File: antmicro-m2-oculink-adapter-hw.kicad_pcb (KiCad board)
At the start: 4 copper layers, 22 x 80 mm, 24 parts, among them J1 PCB-Edge_M.2_Key-M, J2 OCuLink_x4_Amphenol_G14A42121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

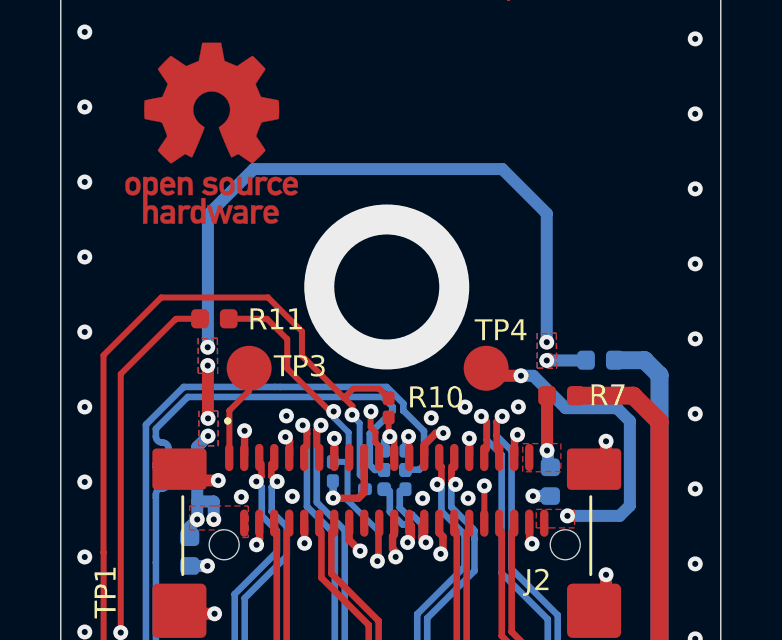
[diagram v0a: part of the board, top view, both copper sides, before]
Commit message: [#81131] Add 0R on 5V, Clean drc
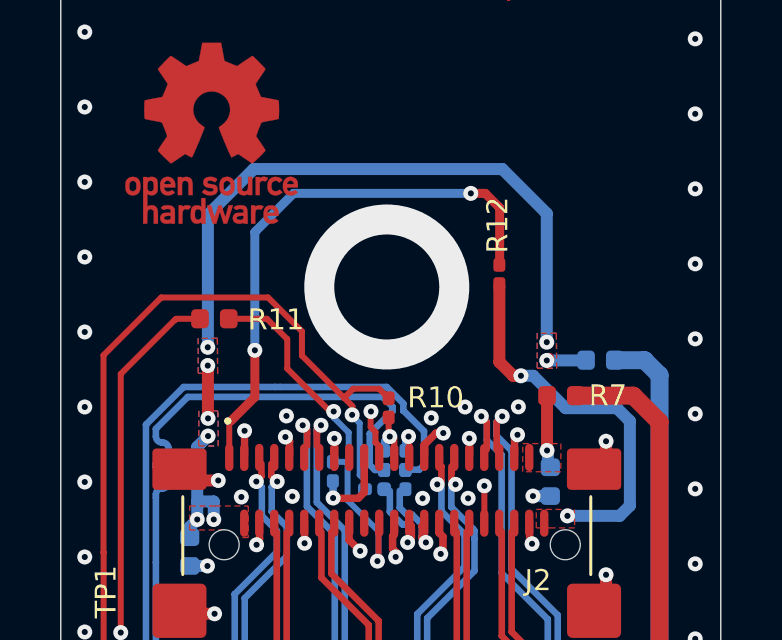
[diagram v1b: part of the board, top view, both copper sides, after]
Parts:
- removed TP3, TP4: TP_1.5mm_SMD, antmicro-footprints:TP_SMD_1.5mm
- added R12: R_0R_0201, antmicro-footprints:R_0201, F.Cu at (149.8, 88.2)
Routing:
- net Net-(J2-5V-PadA21): track 13.8 -> 31.4 mm, vias 2 -> 4

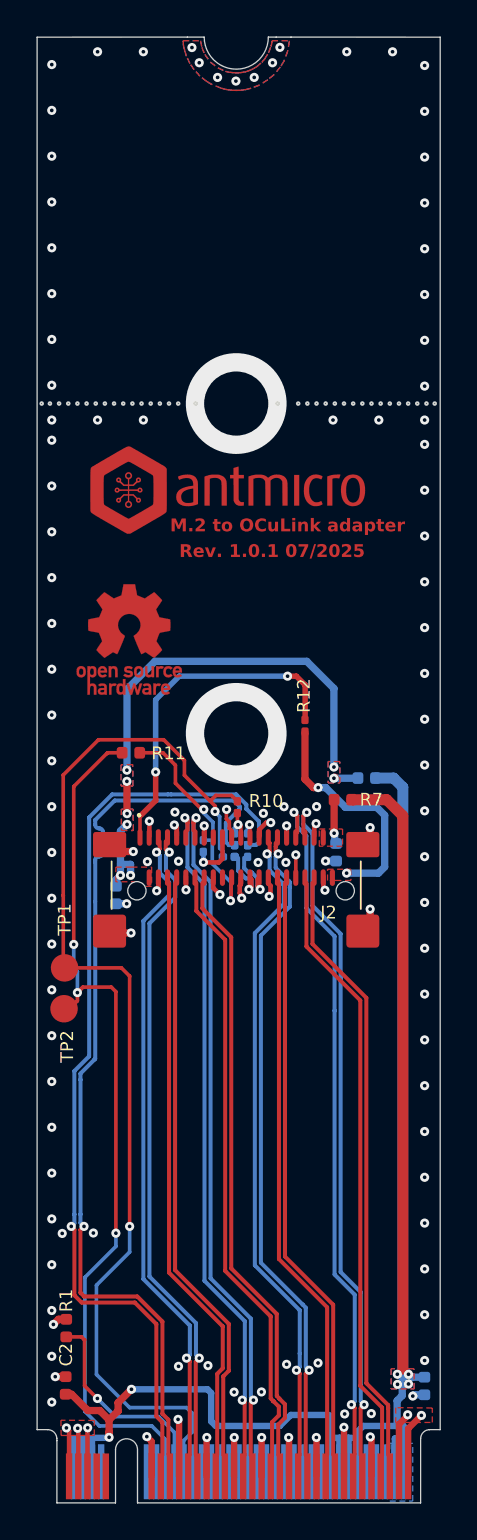
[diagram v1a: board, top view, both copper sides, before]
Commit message: [#81131] Increase silkscreen spacing, add gnd cutouts to vias, increase distance drill to traces, remove solder mask from m.2 connector
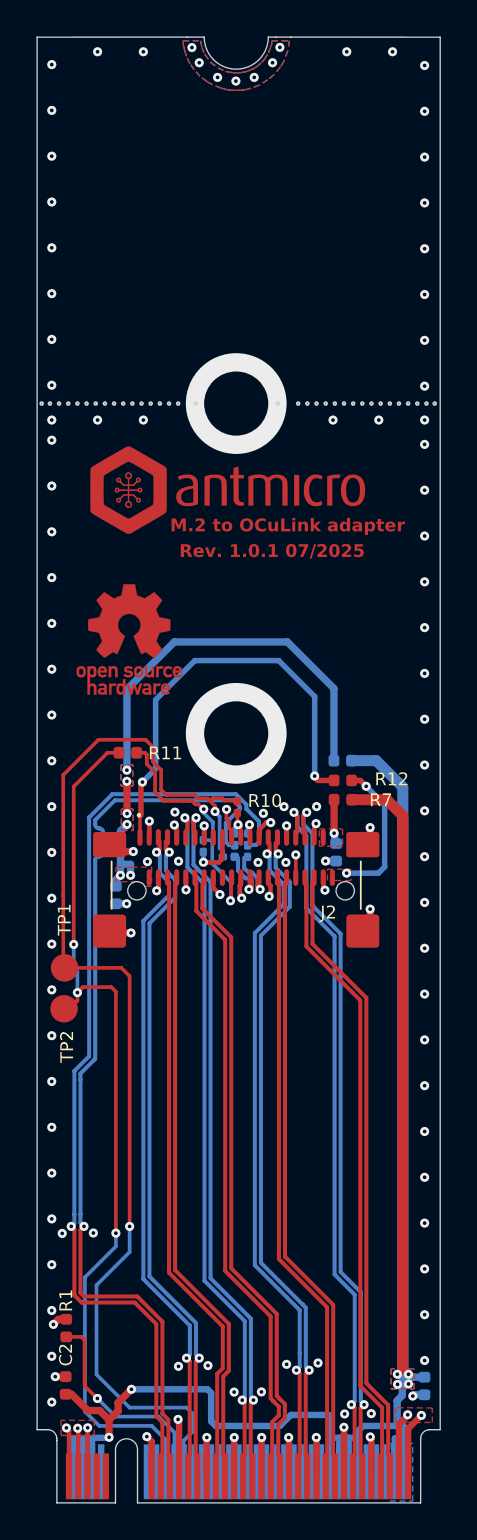
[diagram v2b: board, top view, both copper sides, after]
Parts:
- R12: value R_0R_0201 -> R_0R_0402; footprint antmicro-footprints:R_0201 -> antmicro-footprints:R_0402_1005Metric
- moved R12 3.63 mm to (151.8, 91.2), turned to 180 degrees
- moved R8 1.62 mm to (151.8, 90.1)
- moved R11 0.17 mm to (140.1, 89.7)
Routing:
- net Net-(C1-Pad2): track 115.0 -> 116.4 mm
- net +3V3: track 29.2 -> 28.3 mm, vias 8 -> 6
- net /~{WAKEC}: track 12.8 -> 13.4 mm

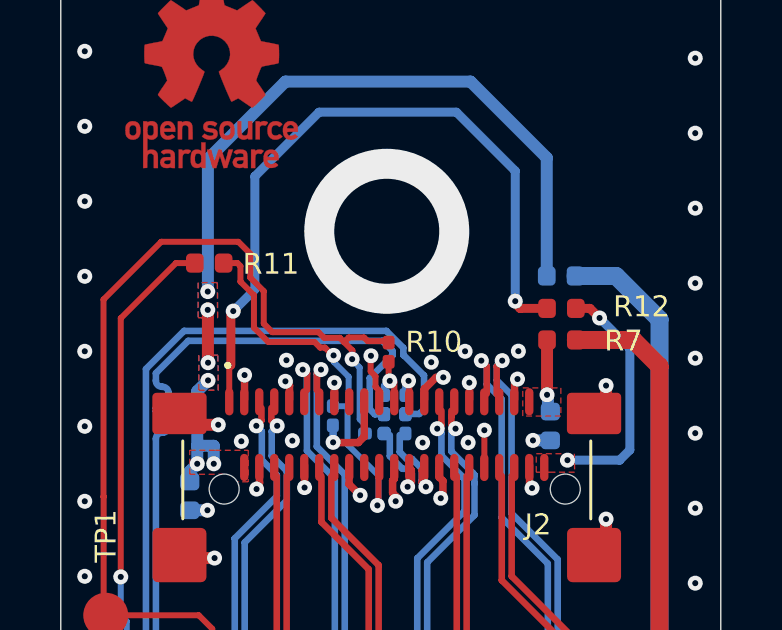
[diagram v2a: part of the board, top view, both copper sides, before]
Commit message: [#81131] remove silkscreen from revision, add testpoint to CPRSNT
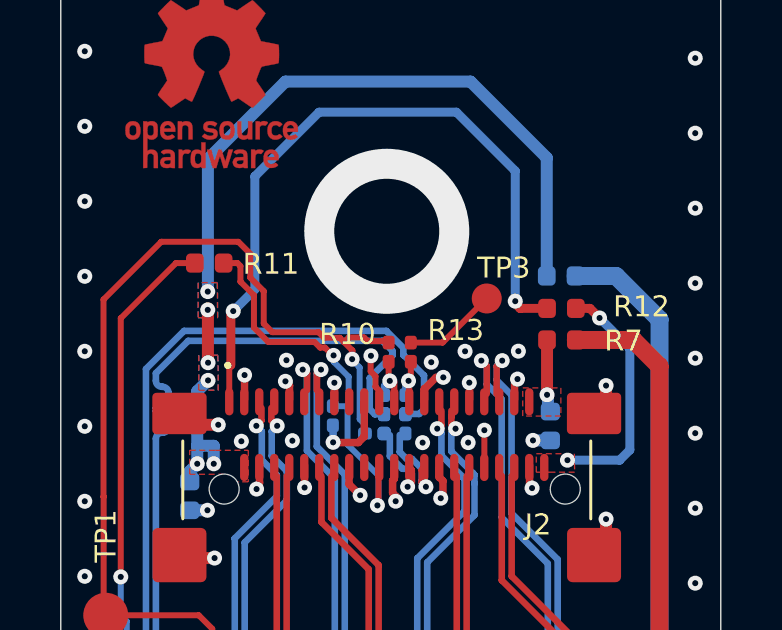
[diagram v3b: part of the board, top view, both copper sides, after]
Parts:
- added R13: R_0R_0201, antmicro-footprints:R_0201, F.Cu at (146.8, 92.6)
- added TP3: TP_1mm_SMD, antmicro-footprints:TP_SMD_1mm, F.Cu at (149.3, 90.8)
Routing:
- net Net-(R13-Pad1): track 0.00 -> 3.14 mm
- net /~{CPRSNT}: track 1.22 -> 1.89 mm

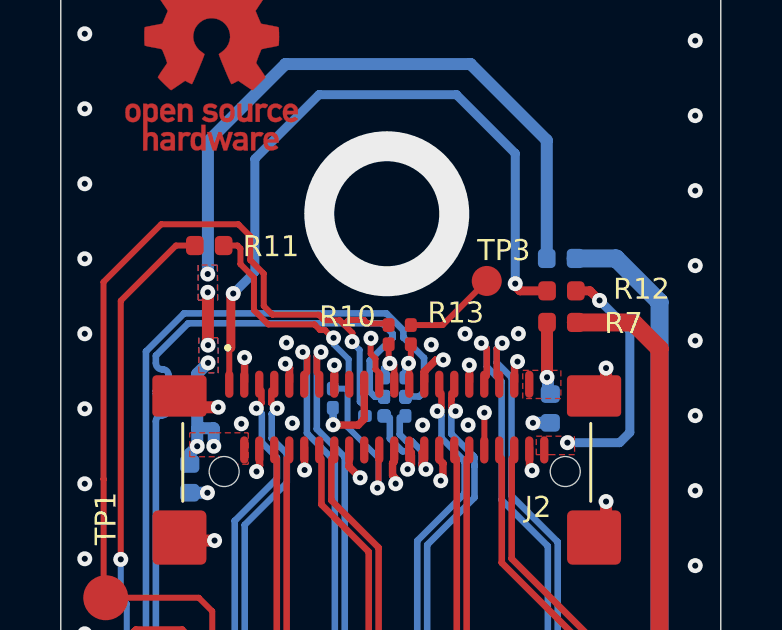
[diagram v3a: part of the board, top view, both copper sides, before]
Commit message: [#81131] Kmake bug workaround
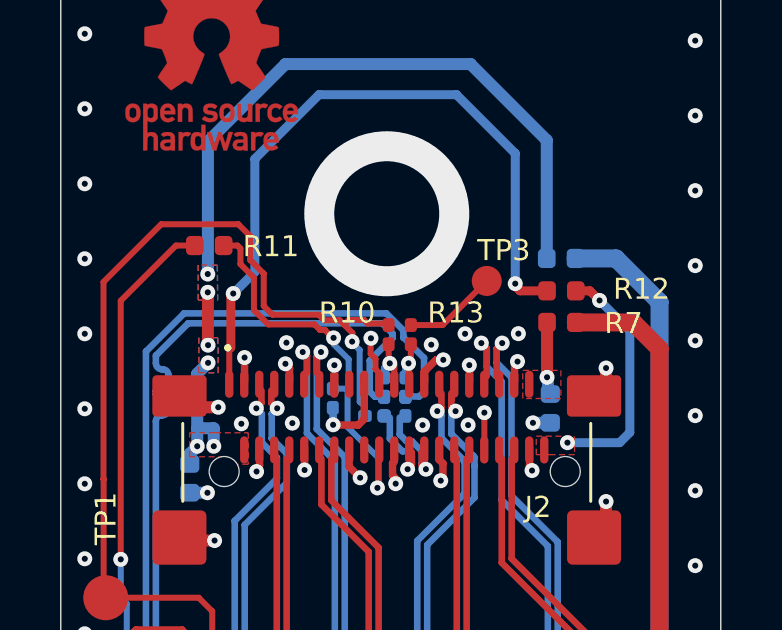
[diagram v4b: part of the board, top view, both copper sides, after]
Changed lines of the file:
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@@
 		(tags "resistor SMD 0201")
 		(property "Reference" "R10"
-			(at -1.01 0.43 180)
+			(at -1.14 0.44 180)
 			(layer "F.SilkS")
 			(effects
@@
 		(net 0)
 		(net_name "")
-		(layers "*.Mask")
+		(layer "F.Mask")
 		(hatch edge 0.5)
 		(connect_pads
@@
 		(polygon
 			(pts
-				(xy 136.16 127.390493) (xy 156.179938 127.409527) (xy 156.16 130.609517) (xy 136.16 130.699517)
+				(xy 136.16 127.881961) (xy 156.176876 127.900992) (xy 156.16 130.609517) (xy 136.16 130.699517)
 			)
 		)
@@
 			)
 		)
+	)
+	(zone
+		(net 0)
+		(net_name "")
+		(layer "B.Mask")
+		(hatch edge 0.5)
+		(connect_pads
+			(clearance 0.2)
+		)
+		(min_thickness 0)
+		(filled_areas_thickness no)
+		(fill yes
+			(thermal_gap 0.5)
+			(thermal_bridge_width 0.5)
+		)
+		(polygon
+			(pts
+				(xy 136.158975 127.390487) (xy 156.178913 127.409521) (xy 156.158975 130.609511) (xy 136.158975 130.699511)
+			)
+		)

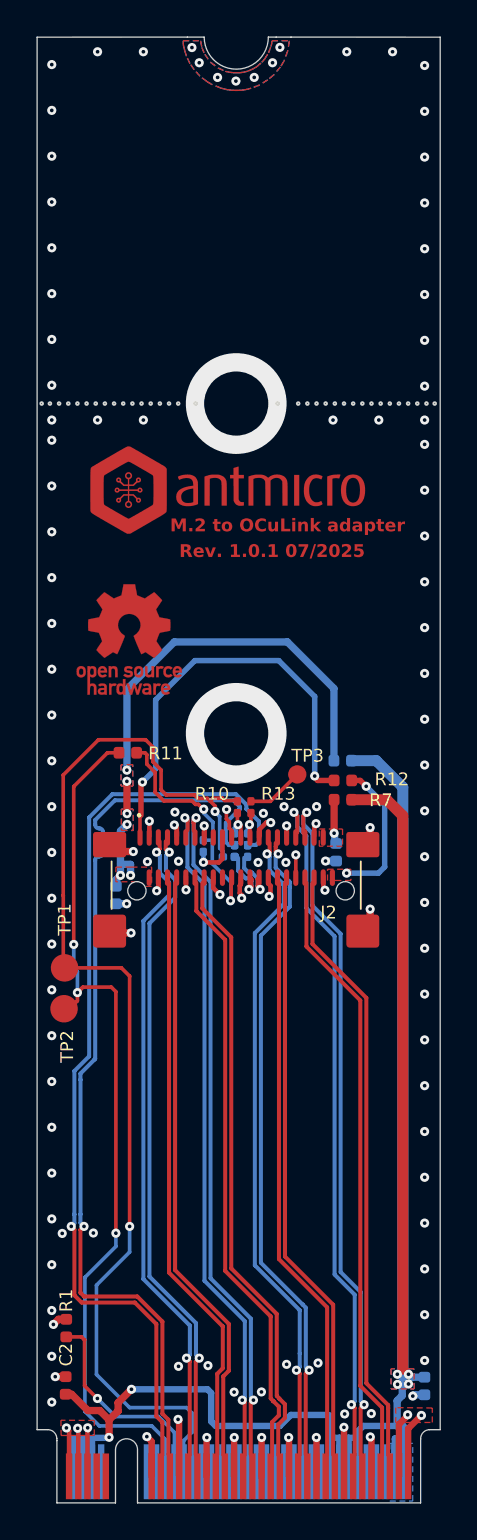
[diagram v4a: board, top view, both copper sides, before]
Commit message: [#81131] Remove plane, adjust silkscreen
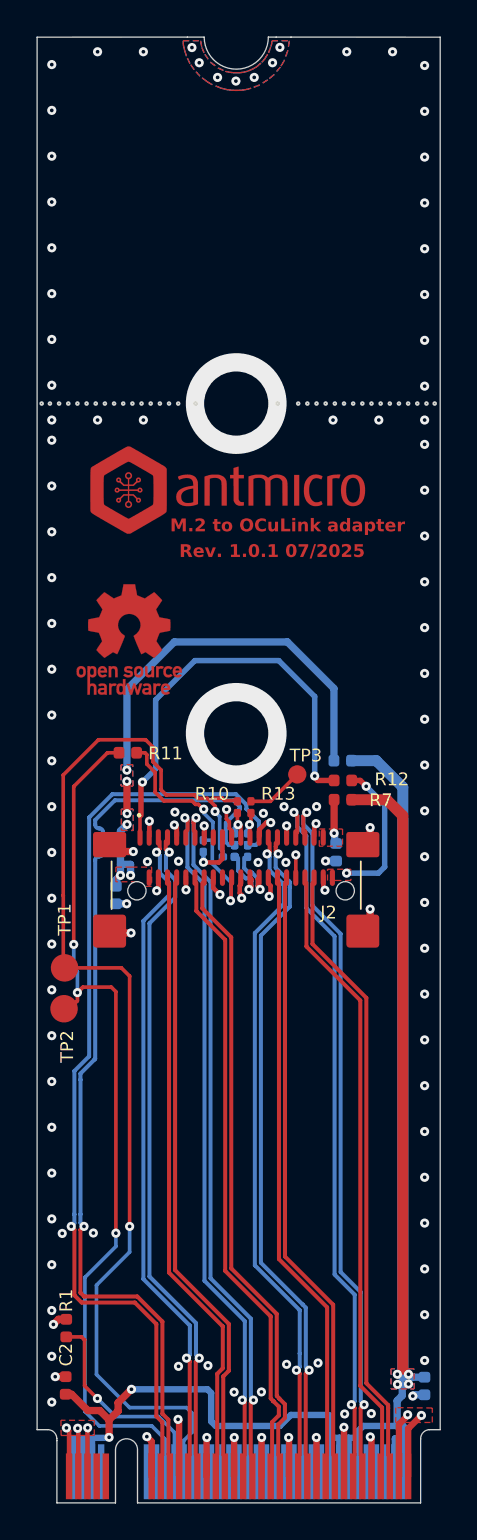
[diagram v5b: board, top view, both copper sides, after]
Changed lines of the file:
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@@
 		(at 149.35 90.84)
 		(property "Reference" "TP3"
-			(at -0.32 -0.61 0)
+			(at -0.42 -0.62 0)
 			(layer "F.SilkS")
 			(effects
@@
 		(tags "capacitor SMD 0402")
 		(property "Reference" "C3"
-			(at 0.48 -1.93 0)
+			(at -0.79 -1.38 270)
 			(layer "B.SilkS")
 			(effects
@@
 		(tags "resistor SMD 0201")
 		(property "Reference" "R9"
-			(at 2.05 -0.77 0)
+			(at -0.79 0.43 90)
 			(layer "B.SilkS")
 			(effects
@@
 		(tags "capacitor SMD 0402")
 		(property "Reference" "C4"
-			(at 0.32 0.47 0)
+			(at -0.72 0.69 90)
 			(layer "B.SilkS")
 			(effects
@@
 			)
 		)
-	)
-	(zone
-		(net 56)
-		(net_name "Net-(C1-Pad2)")
-		(layer "B.Cu")
-		(hatch edge 0.5)
-		(priority 2)
-		(connect_pads yes
-			(clearance 0.16)
-		)
-		(min_thickness 0.25)
-		(filled_areas_thickness no)
-		(fill yes
-			(thermal_gap 0.5)
-			(thermal_bridge_width 0.5)
-		)
-		(polygon
-			(pts
-				(xy 154.4 127.35) (xy 154.4 130.5) (xy 155.65 130.5) (xy 155.65 127.35)
-			)
-		)
